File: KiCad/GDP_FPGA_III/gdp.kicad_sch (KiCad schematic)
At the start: 16 parts, among them J1 NKC-Bus, U2 74LVC245, U3 74LVC245, U4 74LVC245

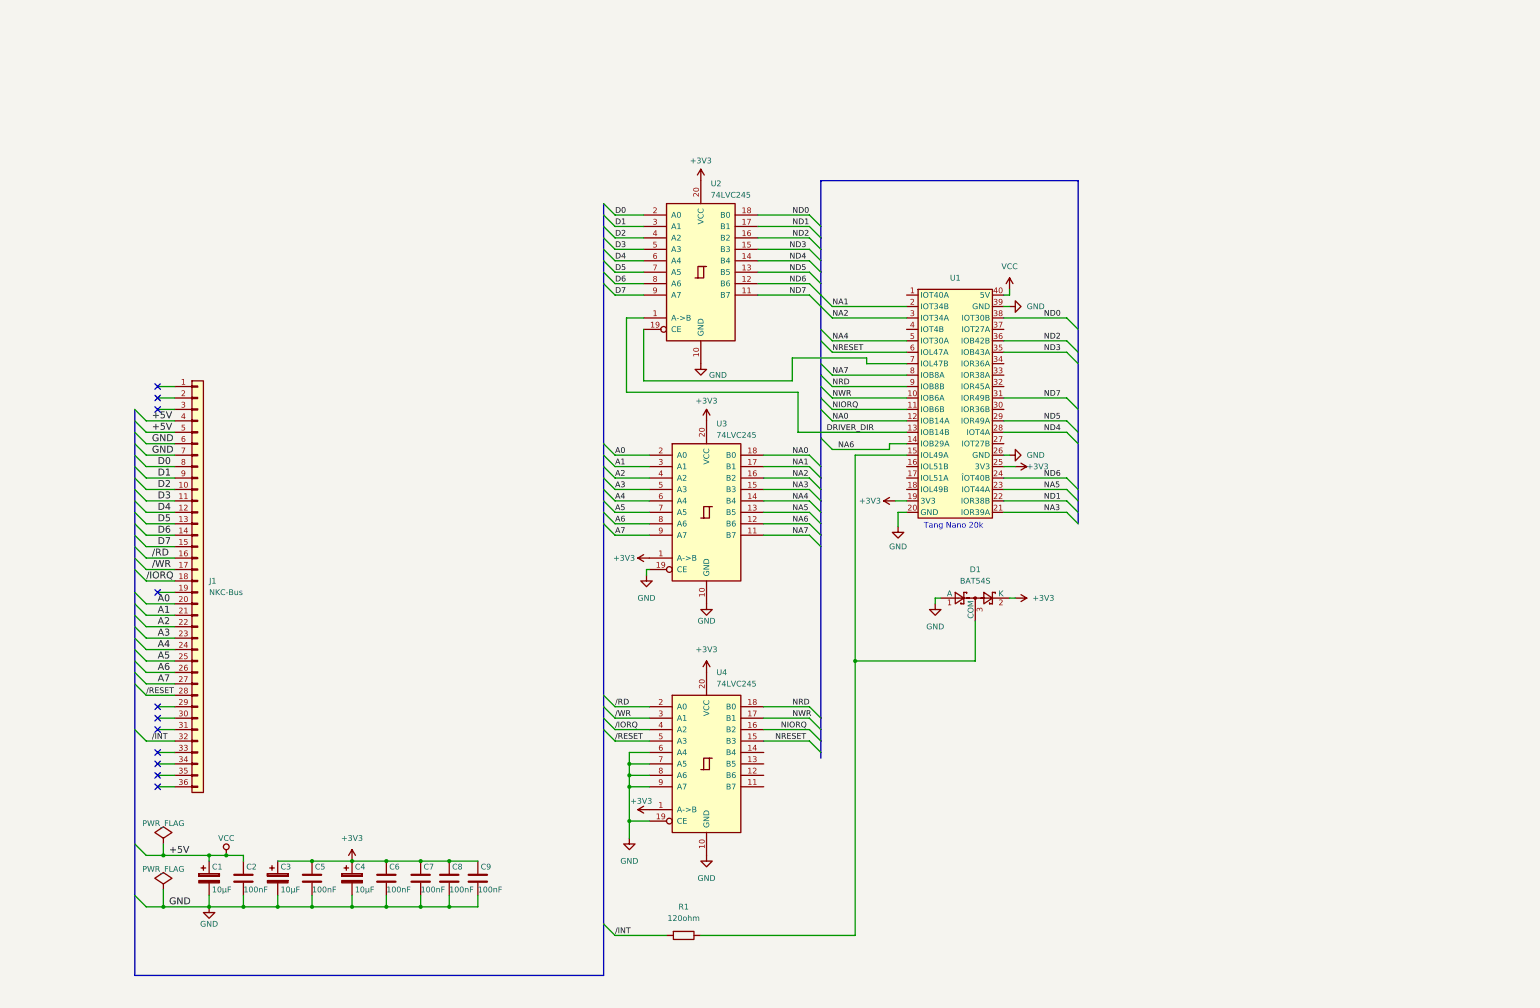
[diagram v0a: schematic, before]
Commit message: update FPGA pin assignement, added PS/2 interfaces
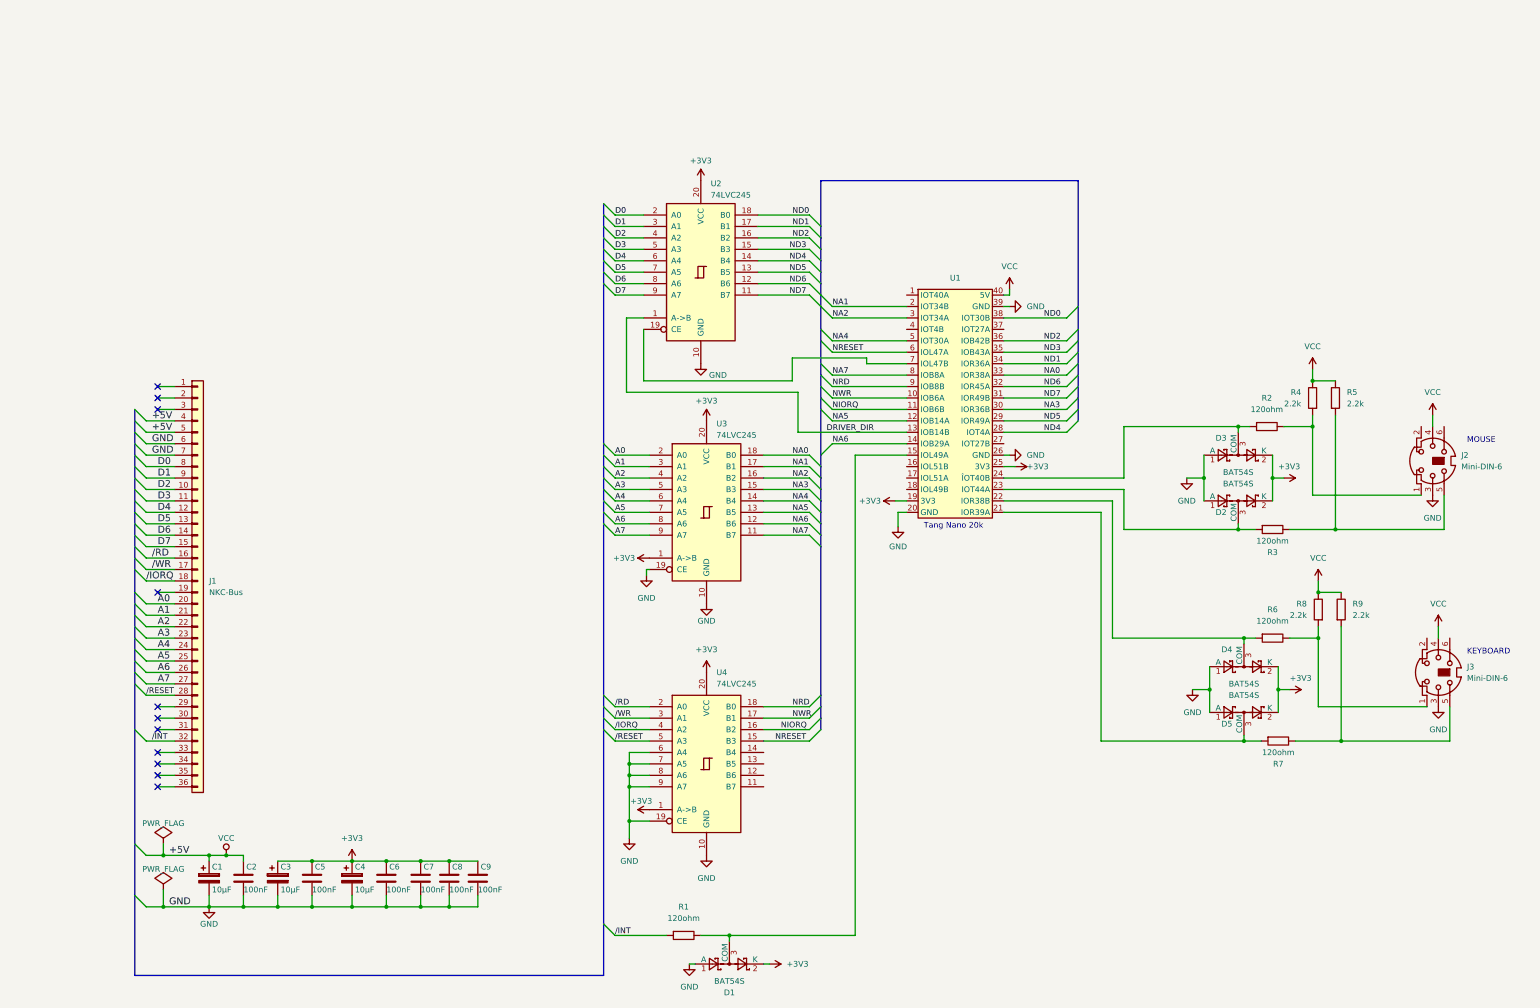
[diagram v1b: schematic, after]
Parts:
- added D2, D3, D4, D5: BAT54S, Package_TO_SOT_SMD:SOT-23, symbol Diode:BAT54S
- added J2, J3: Mini-DIN-6, symbol Connector:Mini-DIN-6
- added R2, R3, R6, R7: 120ohm, Resistor_THT:R_Axial_DIN0207_L6.3mm_D2.5mm_P10.16mm_Horizontal, symbol PCM_SL_Resistors:120ohm
- added R4, R5, R8, R9: 2.2k, Resistor_THT:R_Axial_DIN0207_L6.3mm_D2.5mm_P10.16mm_Horizontal, symbol PCM_SL_Resistors:2.2k
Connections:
- net +3V3: now also D2.2 (K), D3.2 (K), D4.2 (K), D5.2 (K)
- net GND: now also D2.1 (A), D3.1 (A), D4.1 (A), D5.1 (A), J2.3, J3.3
- net NA0: now also U1.33 (IOR38A); no longer U1.12 (IOB14A)
- net NA3: now also U1.30 (IOR36B); no longer U1.21 (IOR39A)
- net NA5: now also U1.12 (IOB14A); no longer U1.23 (IOT44A)
- net ND1: now also U1.34 (IOR36A); no longer U1.22 (IOR38B)
- net ND6: now also U1.32 (IOR45A); no longer U1.24 (ÎOT40B)
- net VCC: now also J2.4, J3.4, R4.2, R5.2, R8.2, R9.2
- new net: D3.3 (COM), R2.1, U1.24 (ÎOT40B)
- new net: J2.1, R2.2, R4.1
- new net: D5.3 (COM), R7.1, U1.21 (IOR39A)
- new net: J2.5, R3.2, R5.1
- new net: D4.3 (COM), R6.1, U1.22 (IOR38B)
- new net: J3.1, R6.2, R8.1
- new net: J3.5, R7.2, R9.1
- new net: D2.3 (COM), R3.1, U1.23 (IOT44A)
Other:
- note added: "KEYBOARD"
- note added: "MOUSE"
- moved on the sheet: D1

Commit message: update
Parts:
- added C10: 4n7, Capacitor_THT:C_Disc_D3.0mm_W2.0mm_P2.50mm, symbol PCM_SL_Devices:Capacitor_NP
- added J4: AudioJack3, Connector_Audio:Jack_3.5mm_CUI_SJ-3524-SMT_Horizontal, symbol Connector_Audio:AudioJack3
- added R10: 3k3, Resistor_THT:R_Axial_DIN0207_L6.3mm_D2.5mm_P10.16mm_Horizontal, symbol PCM_SL_Devices:Resistor
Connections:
- net GND: now also C10.2, J4.T
- net Mouse-Data: now reaches D3.3 (COM), R2.1
- net Mouse-Data: now also U1.22 (IOR38B); no longer U1.24 (ÎOT40B)
- net Keyboard-Clock: now reaches D5.3 (COM), R7.1
- net Keyboard-Clock: now also U1.17 (IOL51A); no longer U1.21 (IOR39A)
- net Keyboard-Data: now reaches D4.3 (COM), R6.1
- net Keyboard-Data: now also U1.18 (IOL49B); no longer U1.22 (IOR38B)
- net Mouse-Clock: now reaches D2.3 (COM), R3.1
- net Mouse-Clock: now also U1.21 (IOR39A); no longer U1.23 (IOT44A)
- new net: C10.1, J4.R, J4.S, R10.2
- new net: R10.1, U1.24 (ÎOT40B)

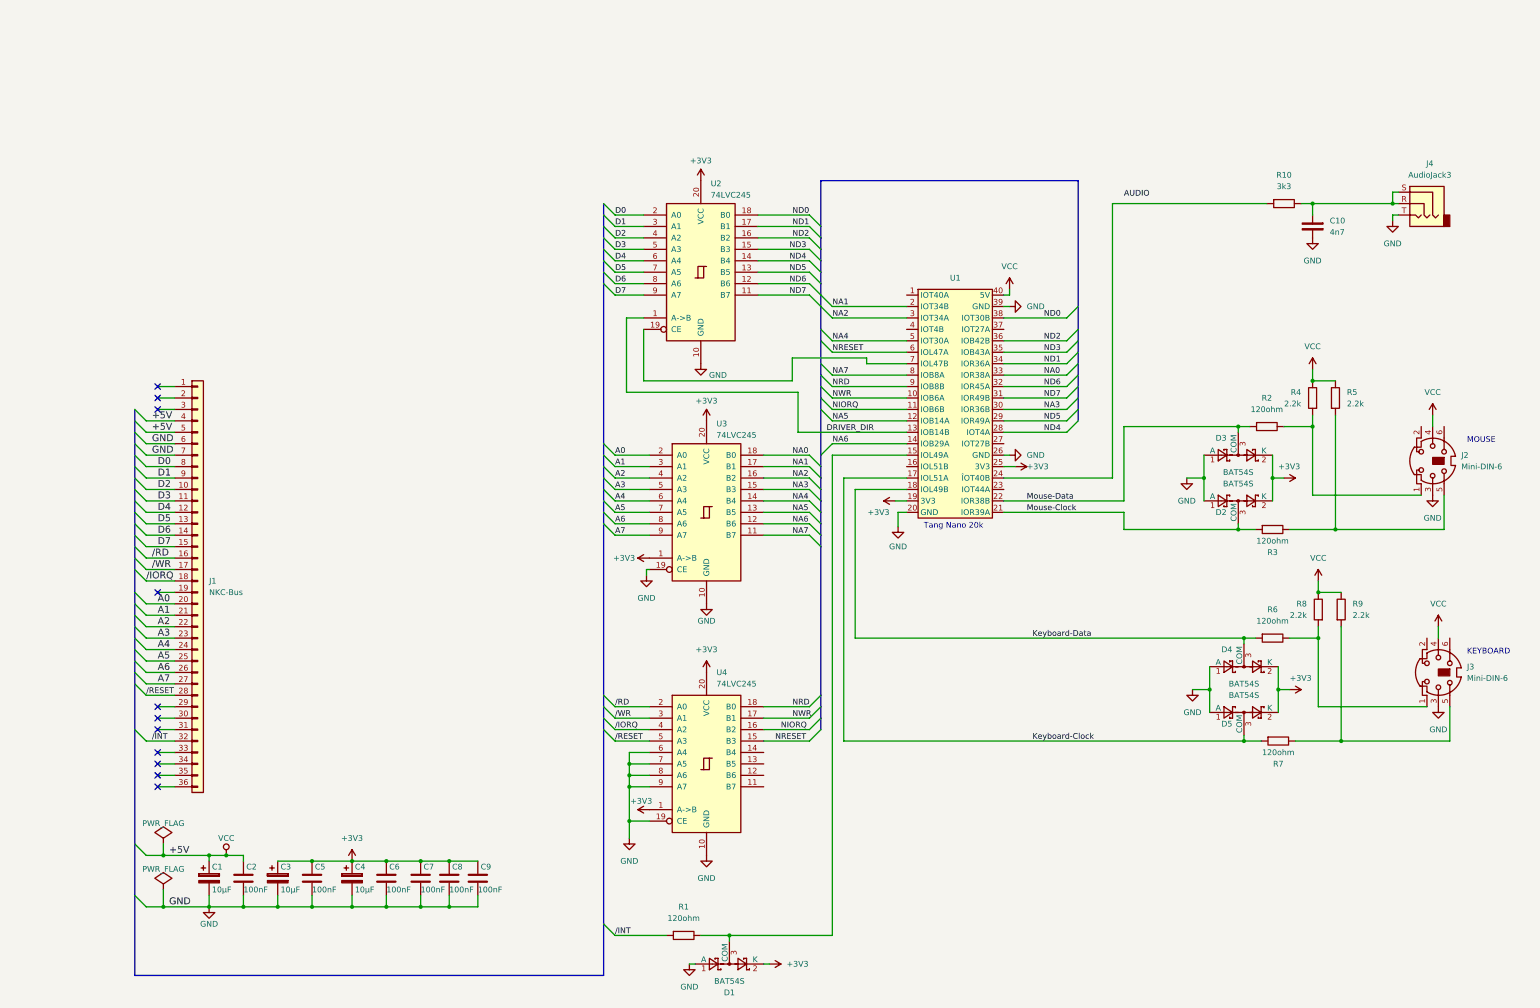
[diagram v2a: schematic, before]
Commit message: NKC inklusive PS2-Key and ext. Businterface
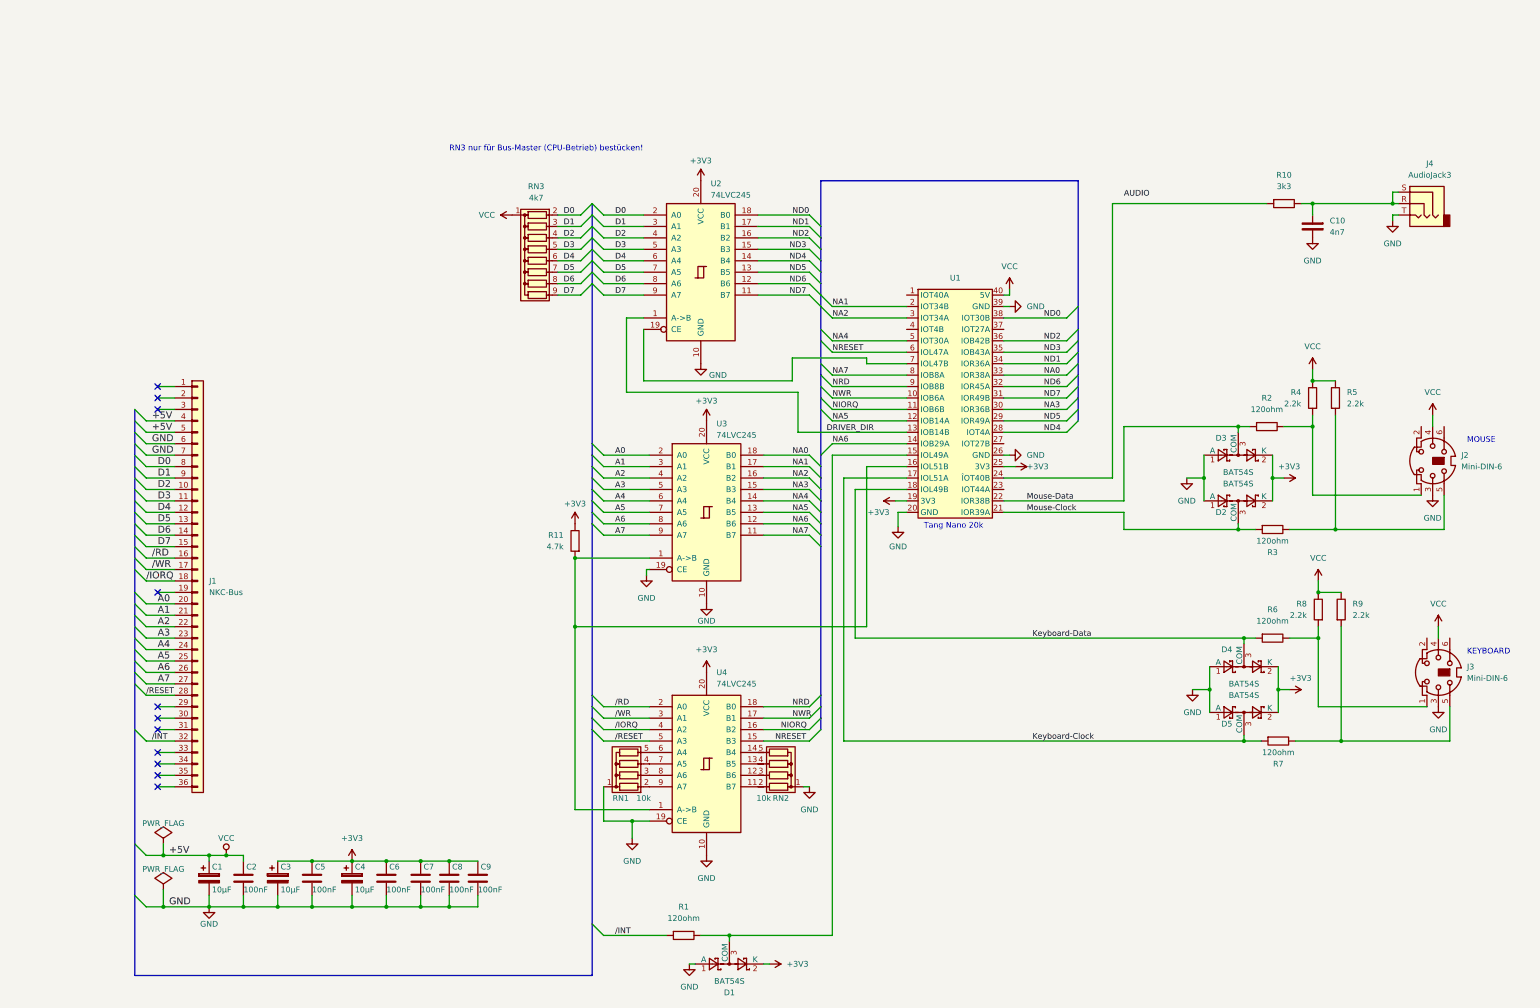
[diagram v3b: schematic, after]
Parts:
- added R11: 4.7k, Resistor_THT:R_Axial_DIN0207_L6.3mm_D2.5mm_P10.16mm_Horizontal, symbol PCM_SL_Resistors:2.2k
- added RN1, RN2: 10k, Resistor_THT:R_Array_SIP5, symbol Device:R_Network04
- added RN3: 4k7, Resistor_THT:R_Array_SIP9, symbol Device:R_Network08
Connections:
- net +3V3: now also R11.2; no longer U3.1 (A->B), U4.1 (A->B)
- net D0: now also RN3.2 (R1)
- net D1: now also RN3.3 (R2)
- net D2: now also RN3.4 (R3)
- net D3: now also RN3.5 (R4)
- net D4: now also RN3.6 (R5)
- net D5: now also RN3.7 (R6)
- net D6: now also RN3.8 (R7)
- net D7: now also RN3.9 (R8)
- net GND: now also RN1.1 (common), RN2.1 (common); no longer U4.6 (A4), U4.7 (A5), U4.8 (A6), U4.9 (A7)
- net VCC: now also RN3.1 (common)
- net at U1.16 (IOL51B): now also U3.1 (A->B), U4.1 (A->B), R11.1
- new net: RN1.5 (R4), U4.6 (A4)
- new net: RN1.4 (R3), U4.7 (A5)
- new net: RN1.3 (R2), U4.8 (A6)
- new net: RN1.2 (R1), U4.9 (A7)
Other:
- note added: "RN3 nur für Bus-Master (CPU-Betrieb) bestücken!"
